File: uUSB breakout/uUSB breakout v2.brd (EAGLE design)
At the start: 13.3 x 16.5 mm, 12 parts

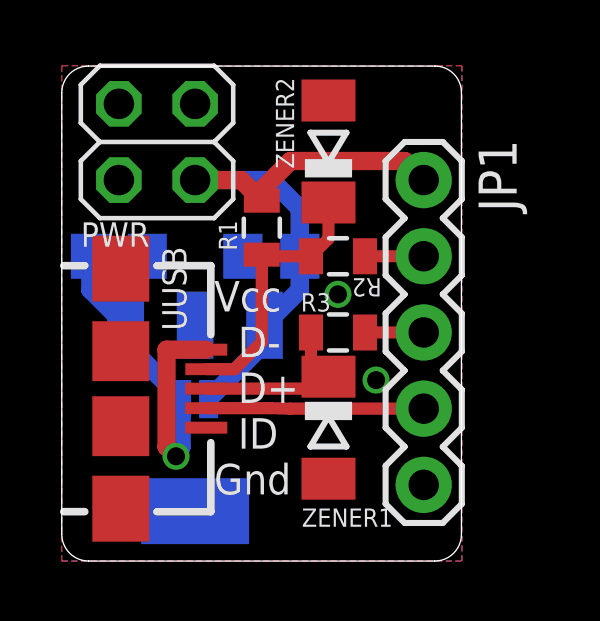
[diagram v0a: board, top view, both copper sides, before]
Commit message: added some info to silk screen
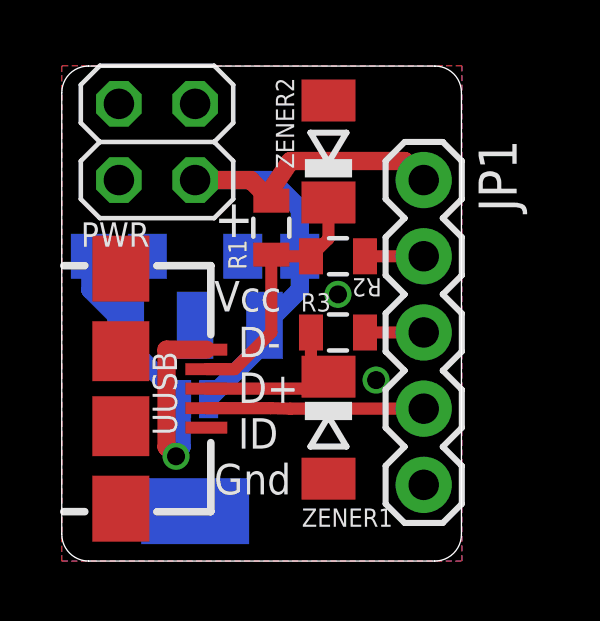
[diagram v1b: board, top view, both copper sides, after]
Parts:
- moved R1 0.32 mm to (6.99, 11.7)
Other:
- board text added: "+"
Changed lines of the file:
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@@
 ID
 Gnd</text>
+<text x="5.08" y="11.43" size="1.27" layer="25">+</text>
 </plain>
 <attributes>
@@
 <elements>
 <element name="UUSB" library="SparkFun-Connectors" package="USB-AB-MICRO-SMD" value="" x="1.9685" y="6.38175" smashed="yes">
-<attribute name="NAME" x="4.15925" y="8.3185" size="0.8128" layer="25" rot="R90"/>
+<attribute name="NAME" x="3.84175" y="4.826" size="0.8128" layer="25" rot="R90"/>
 <attribute name="VALUE" x="0.6985" y="11.84275" size="0.4064" layer="27"/>
 </element>
@@
 <attribute name="VALUE" x="7.62" y="12.065" size="1.27" layer="27" rot="R90"/>
 </element>
-<element name="R1" library="SparkFun-Passives" package="0805" value="1.5k" x="6.6675" y="11.7475" smashed="yes" rot="R90">
-<attribute name="NAME" x="5.842" y="10.9855" size="0.6096" layer="25" rot="R90"/>
-<attribute name="VALUE" x="6.25475" y="11.52525" size="0.4064" layer="27"/>
+<element name="R1" library="SparkFun-Passives" package="0805" value="1.5k" x="6.985" y="11.7475" smashed="yes" rot="R90">
+<attribute name="NAME" x="6.1595" y="10.3505" size="0.6096" layer="25" rot="R90"/>
+<attribute name="VALUE" x="6.57225" y="11.52525" size="0.4064" layer="27"/>
 </element>
 <element name="R2" library="SparkFun-Passives" package="0805" value="68" x="9.2075" y="10.795" smashed="yes">
@@
 <contactref element="ZENER2" pad="C"/>
 <wire x1="4.8185" y1="7.03175" x2="5.76175" y2="7.03175" width="0.4064" layer="1"/>
-<wire x1="5.76175" y1="7.03175" x2="6.6675" y2="7.9375" width="0.4064" layer="1"/>
-<wire x1="6.6675" y1="7.9375" x2="6.6675" y2="10.8475" width="0.4064" layer="1"/>
-<wire x1="6.6675" y1="10.8475" x2="6.72" y2="10.795" width="0.4064" layer="1"/>
+<wire x1="5.76175" y1="7.03175" x2="6.985" y2="8.255" width="0.4064" layer="1"/>
+<wire x1="6.985" y1="8.255" x2="6.985" y2="10.8475" width="0.4064" layer="1"/>
+<wire x1="6.985" y1="10.8475" x2="6.72" y2="10.795" width="0.4064" layer="1"/>
 <wire x1="6.72" y1="10.795" x2="8.3075" y2="10.795" width="0.4064" layer="1"/>
 <wire x1="8.89" y1="12.5875" x2="8.89" y2="11.3775" width="0.4064" layer="1"/>
@@
 <wire x1="12.065" y1="13.335" x2="11.43" y2="13.97" width="0.6096" layer="1"/>
 <wire x1="11.43" y1="13.97" x2="7.62" y2="13.97" width="0.6096" layer="1"/>
-<wire x1="7.62" y1="13.97" x2="6.6675" y2="13.0175" width="0.6096" layer="1"/>
-<wire x1="6.6675" y1="13.0175" x2="6.6675" y2="12.6475" width="0.6096" layer="1"/>
-<wire x1="4.445" y1="13.335" x2="5.98" y2="13.335" width="0.6096" layer="1"/>
-<wire x1="5.98" y1="13.335" x2="6.6675" y2="12.6475" width="0.6096" layer="1"/>
+<wire x1="7.62" y1="13.97" x2="6.985" y2="13.0175" width="0.6096" layer="1"/>
+<wire x1="6.985" y1="13.0175" x2="6.985" y2="12.6475" width="0.6096" layer="1"/>
+<wire x1="4.445" y1="13.335" x2="6.2975" y2="13.335" width="0.6096" layer="1"/>
+<wire x1="6.2975" y1="13.335" x2="6.985" y2="12.6475" width="0.6096" layer="1"/>
 <contactref element="SJ1" pad="2"/>
 <wire x1="7.935" y1="10.795" x2="7.935" y2="9.6749" width="0.6096" layer="16"/>

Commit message: updated .brd
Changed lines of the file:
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@@
 <layer number="99" name="SpiceOrder" color="7" fill="1" visible="no" active="no"/>
 <layer number="100" name="Muster" color="7" fill="1" visible="no" active="no"/>
-<layer number="101" name="Patch_Top" color="12" fill="4" visible="yes" active="yes"/>
-<layer number="102" name="Vscore" color="7" fill="1" visible="yes" active="yes"/>
-<layer number="103" name="tMap" color="7" fill="1" visible="yes" active="yes"/>
-<layer number="104" name="Name" color="16" fill="1" visible="yes" active="yes"/>
-<layer number="105" name="tPlate" color="7" fill="1" visible="yes" active="yes"/>
-<layer number="106" name="bPlate" color="7" fill="1" visible="yes" active="yes"/>
-<layer number="107" name="Crop" color="7" fill="1" visible="yes" active="yes"/>
-<layer number="108" name="tplace-old" color="10" fill="1" visible="yes" active="yes"/>
-<layer number="109" name="ref-old" color="11" fill="1" visible="yes" active="yes"/>
-<layer number="110" name="fp0" color="7" fill="1" visible="yes" active="yes"/>
-<layer number="111" name="LPC17xx" color="7" fill="1" visible="yes" active="yes"/>
-<layer number="112" name="tSilk" color="7" fill="1" visible="yes" active="yes"/>
-<layer number="113" name="IDFDebug" color="4" fill="1" visible="yes" active="yes"/>
-<layer number="116" name="Patch_BOT" color="9" fill="4" visible="yes" active="yes"/>
+<layer number="101" name="Patch_Top" color="12" fill="4" visible="no" active="yes"/>
+<layer number="102" name="Vscore" color="7" fill="1" visible="no" active="yes"/>
+<layer number="103" name="tMap" color="7" fill="1" visible="no" active="yes"/>
+<layer number="104" name="Name" color="16" fill="1" visible="no" active="yes"/>
+<layer number="105" name="tPlate" color="7" fill="1" visible="no" active="yes"/>
+<layer number="106" name="bPlate" color="7" fill="1" visible="no" active="yes"/>
+<layer number="107" name="Crop" color="7" fill="1" visible="no" active="yes"/>
+<layer number="108" name="tplace-old" color="10" fill="1" visible="no" active="yes"/>
+<layer number="109" name="ref-old" color="11" fill="1" visible="no" active="yes"/>
+<layer number="110" name="fp0" color="7" fill="1" visible="no" active="yes"/>
+<layer number="111" name="LPC17xx" color="7" fill="1" visible="no" active="yes"/>
+<layer number="112" name="tSilk" color="7" fill="1" visible="no" active="yes"/>
+<layer number="113" name="IDFDebug" color="4" fill="1" visible="no" active="yes"/>
+<layer number="116" name="Patch_BOT" color="9" fill="4" visible="no" active="yes"/>
 <layer number="118" name="Rect_Pads" color="7" fill="1" visible="no" active="no"/>
-<layer number="121" name="_tsilk" color="7" fill="1" visible="yes" active="yes"/>
-<layer number="122" name="_bsilk" color="7" fill="1" visible="yes" active="yes"/>
-<layer number="123" name="tTestmark" color="7" fill="1" visible="yes" active="yes"/>
-<layer number="124" name="bTestmark" color="7" fill="1" visible="yes" active="yes"/>
-<layer number="125" name="_tNames" color="7" fill="1" visible="yes" active="yes"/>
-<layer number="126" name="_bNames" color="7" fill="1" visible="yes" active="yes"/>
-<layer number="127" name="_tValues" color="7" fill="1" visible="yes" active="yes"/>
-<layer number="128" name="_bValues" color="7" fill="1" visible="yes" active="yes"/>
-<layer number="131" name="tAdjust" color="7" fill="1" visible="yes" active="yes"/>
-<layer number="132" name="bAdjust" color="7" fill="1" visible="yes" active="yes"/>
-<layer number="144" name="Drill_legend" color="7" fill="1" visible="yes" active="yes"/>
-<layer number="150" name="Notes" color="7" fill="1" visible="yes" active="yes"/>
-<layer number="151" name="HeatSink" color="7" fill="1" visible="yes" active="yes"/>
-<layer number="152" name="_bDocu" color="7" fill="1" visible="yes" active="yes"/>
-<layer number="153" name="FabDoc1" color="7" fill="1" visible="yes" active="yes"/>
-<layer number="154" name="FabDoc2" color="7" fill="1" visible="yes" active="yes"/>
-<layer number="155" name="FabDoc3" color="7" fill="1" visible="yes" active="yes"/>
-<layer number="199" name="Contour" color="7" fill="1" visible="yes" active="yes"/>
-<layer number="200" name="200bmp" color="1" fill="10" visible="yes" active="yes"/>
-<layer number="201" name="201bmp" color="2" fill="10" visible="yes" active="yes"/>
-<layer number="202" name="202bmp" color="3" fill="10" visible="yes" active="yes"/>
-<layer number="203" name="203bmp" color="4" fill="10" visible="yes" active="yes"/>
-<layer number="204" name="204bmp" color="5" fill="10" visible="yes" active="yes"/>
-<layer number="205" name="205bmp" color="6" fill="10" visible="yes" active="yes"/>
-<layer number="206" name="206bmp" color="7" fill="10" visible="yes" active="yes"/>
-<layer number="207" name="207bmp" color="8" fill="10" visible="yes" active="yes"/>
-<layer number="208" name="208bmp" color="9" fill="10" visible="yes" active="yes"/>
-<layer number="209" name="209bmp" color="7" fill="1" visible="yes" active="yes"/>
-<layer number="210" name="210bmp" color="7" fill="1" visible="yes" active="yes"/>
-<layer number="211" name="211bmp" color="7" fill="1" visible="yes" active="yes"/>
-<layer number="212" name="212bmp" color="7" fill="1" visible="yes" active="yes"/>
-<layer number="213" name="213bmp" color="7" fill="1" visible="yes" active="yes"/>
-<layer number="214" name="214bmp" color="7" fill="1" visible="yes" active="yes"/>
-<layer number="215" name="215bmp" color="7" fill="1" visible="yes" active="yes"/>
-<layer number="216" name="216bmp" color="7" fill="1" visible="yes" active="yes"/>
+<layer number="121" name="_tsilk" color="7" fill="1" visible="no" active="yes"/>
+<layer number="122" name="_bsilk" color="7" fill="1" visible="no" active="yes"/>
+<layer number="123" name="tTestmark" color="7" fill="1" visible="no" active="yes"/>
+<layer number="124" name="bTestmark" color="7" fill="1" visible="no" active="yes"/>
+<layer number="125" name="_tNames" color="7" fill="1" visible="no" active="yes"/>
+<layer number="126" name="_bNames" color="7" fill="1" visible="no" active="yes"/>
+<layer number="127" name="_tValues" color="7" fill="1" visible="no" active="yes"/>
+<layer number="128" name="_bValues" color="7" fill="1" visible="no" active="yes"/>
+<layer number="131" name="tAdjust" color="7" fill="1" visible="no" active="yes"/>
+<layer number="132" name="bAdjust" color="7" fill="1" visible="no" active="yes"/>
+<layer number="144" name="Drill_legend" color="7" fill="1" visible="no" active="yes"/>
+<layer number="150" name="Notes" color="7" fill="1" visible="no" active="yes"/>
+<layer number="151" name="HeatSink" color="7" fill="1" visible="no" active="yes"/>
+<layer number="152" name="_bDocu" color="7" fill="1" visible="no" active="yes"/>
+<layer number="153" name="FabDoc1" color="7" fill="1" visible="no" active="yes"/>
+<layer number="154" name="FabDoc2" color="7" fill="1" visible="no" active="yes"/>
+<layer number="155" name="FabDoc3" color="7" fill="1" visible="no" active="yes"/>
+<layer number="199" name="Contour" color="7" fill="1" visible="no" active="yes"/>
+<layer number="200" name="200bmp" color="1" fill="10" visible="no" active="yes"/>
+<layer number="201" name="201bmp" color="2" fill="10" visible="no" active="yes"/>
+<layer number="202" name="202bmp" color="3" fill="10" visible="no" active="yes"/>
+<layer number="203" name="203bmp" color="4" fill="10" visible="no" active="yes"/>
+<layer number="204" name="204bmp" color="5" fill="10" visible="no" active="yes"/>
+<layer number="205" name="205bmp" color="6" fill="10" visible="no" active="yes"/>
+<layer number="206" name="206bmp" color="7" fill="10" visible="no" active="yes"/>
+<layer number="207" name="207bmp" color="8" fill="10" visible="no" active="yes"/>
+<layer number="208" name="208bmp" color="9" fill="10" visible="no" active="yes"/>
+<layer number="209" name="209bmp" color="7" fill="1" visible="no" active="yes"/>
+<layer number="210" name="210bmp" color="7" fill="1" visible="no" active="yes"/>
+<layer number="211" name="211bmp" color="7" fill="1" visible="no" active="yes"/>
+<layer number="212" name="212bmp" color="7" fill="1" visible="no" active="yes"/>
+<layer number="213" name="213bmp" color="7" fill="1" visible="no" active="yes"/>
+<layer number="214" name="214bmp" color="7" fill="1" visible="no" active="yes"/>
+<layer number="215" name="215bmp" color="7" fill="1" visible="no" active="yes"/>
+<layer number="216" name="216bmp" color="7" fill="1" visible="no" active="yes"/>
 <layer number="217" name="217bmp" color="18" fill="1" visible="no" active="no"/>
 <layer number="218" name="218bmp" color="19" fill="1" visible="no" active="no"/>
@@
 <layer number="232" name="Eagle3D_PG2" color="7" fill="1" visible="no" active="no"/>
 <layer number="233" name="Eagle3D_PG3" color="7" fill="1" visible="no" active="no"/>
-<layer number="248" name="Housing" color="7" fill="1" visible="yes" active="yes"/>
-<layer number="249" name="Edge" color="7" fill="1" visible="yes" active="yes"/>
+<layer number="248" name="Housing" color="7" fill="1" visible="no" active="yes"/>
+<layer number="249" name="Edge" color="7" fill="1" visible="no" active="yes"/>
 <layer number="250" name="Descript" color="3" fill="1" visible="no" active="no"/>
 <layer number="251" name="SMDround" color="12" fill="11" visible="no" active="no"/>
-<layer number="254" name="cooling" color="7" fill="1" visible="yes" active="yes"/>
-<layer number="255" name="routoute" color="7" fill="1" visible="yes" active="yes"/>
+<layer number="254" name="cooling" color="7" fill="1" visible="no" active="yes"/>
+<layer number="255" name="routoute" color="7" fill="1" visible="no" active="yes"/>
 </layers>
 <board>
@@
 <via x="10.4775" y="6.6675" extent="1-16" drill="0.6"/>
 <via x="9.2075" y="9.525" extent="1-16" drill="0.6"/>
+<via x="6.6675" y="4.445" extent="1-16" drill="0.6"/>
+<via x="4.445" y="10.795" extent="1-16" drill="0.6"/>
+<via x="10.4775" y="12.065" extent="1-16" drill="0.6"/>
+<via x="6.6675" y="14.605" extent="1-16" drill="0.6"/>
 </signal>
 <signal name="N$1">
